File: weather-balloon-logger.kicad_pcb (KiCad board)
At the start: 2 copper layers, 80 x 70 mm, 22 parts, among them J1 Conn_01x02, J2 Conn_01x11, J3 SMA, J4 SMA, J5 Conn_01x02, J6 VHF, J7 HF, Q1 AO3400A, SW1 SPDT, U1 PCF8574T

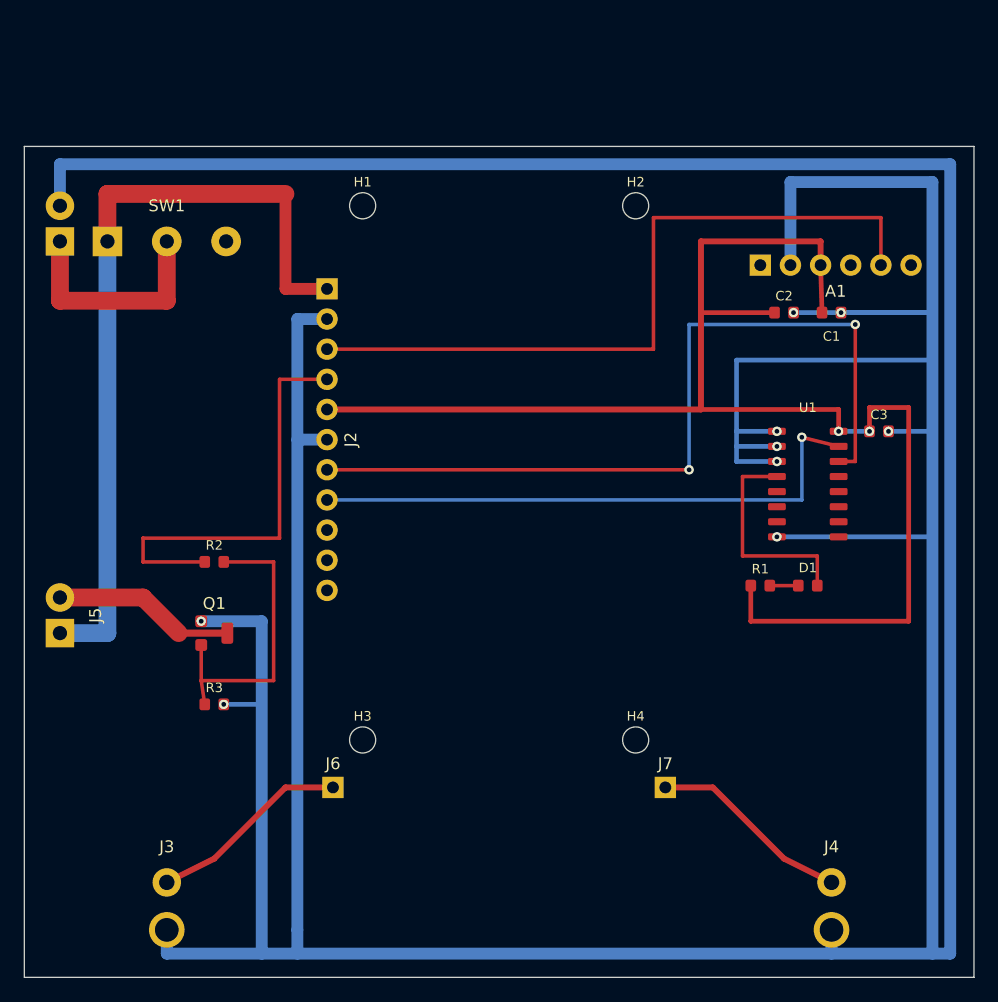
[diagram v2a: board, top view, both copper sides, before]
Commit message: copperhead: Correct the module-mount layout to the exact verified LightAPRS-W 2.0 geometry and FACE-UP orientation in docs/SUBSYSTEMS.md section 6. (1) Resize the module-mount zone to exactly 32.77 x 54.80 mm with the long axis vertical. (2) The module mounts FACE UP, so carrier pads must match the module top view with NO left-right mirror: place J2 (11-pin header) on the zone edge that matches the module's header edge, and place the RF corner contacts as HF bottom-left = J7 and VHF bottom-right = J6, which reverses the previous mirrored placement. (3) Keep RF nets VHF/J6 -> J3 (RF_APRS) and HF/J7 -> J4 (RF_WSPR); the two SMA jacks are edge-mounted facing down, so move J3 toward the VHF/right side and J4 toward the HF/left side for short launches. (4) Place four approximate M2 standoff holes on the dimensioned pattern with about a 42.73 mm outer horizontal span. (5) Keep J1, SW1, A1, U1, C3, Q1 and all passives outside the module zone and honor the >=5 mm SMA keepouts. Update docs/LAYOUT.md and the board, then re-run DRC.
Corrected the LightAPRS-W 2.0 carrier layout to the exact 32.77 x 54.80 mm FACE-UP module zone with its long axis vertical. J2 is on the matching right-hand header edge without mirroring; J7/HF is bottom-left feeding left-side J4/RF_WSPR, and J6/VHF is bottom-right feeding right-side J3/RF_APRS. Four approximate M2 holes use the vendor drawing's about 42.73 mm long-axis span rotated onto the PCB vertical axis. All non-mating components remain outside the zone, both SMA envelopes retain at least 5 mm clearance, documentation and constraints are synchronized, DRC and drift are clean, and the board SVG was refreshed. Draft footprints, exact hole offsets, RF stackup/launches, and physical fit remain explicit fabrication holds.

Verification: ERC clean, DRC clean
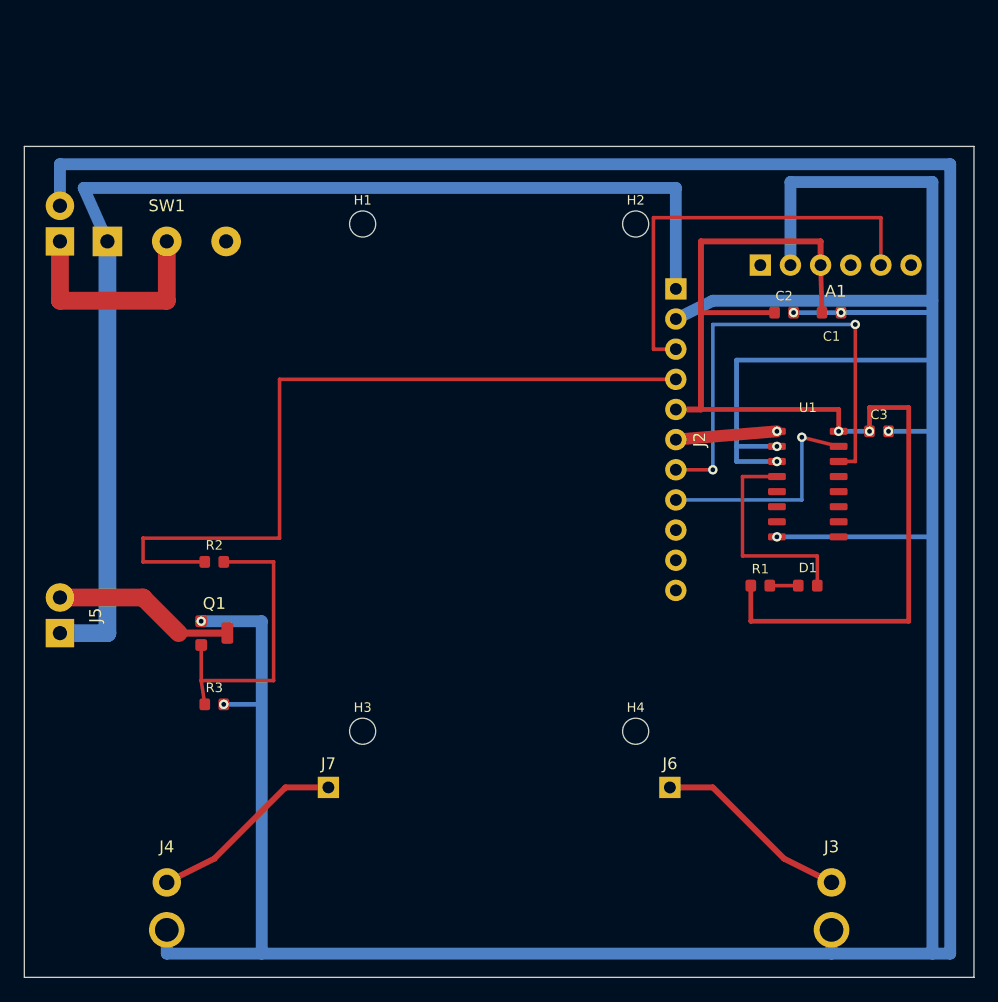
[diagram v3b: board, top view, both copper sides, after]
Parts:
- moved J3 56.0 mm to (168.0, 162.0)
- moved J4 56.0 mm to (112.0, 162.0)
- moved J2 29.4 mm to (154.9, 112.0)
- moved J7 28.4 mm to (125.6, 154.0)
- moved J6 28.4 mm to (154.4, 154.0)
- moved H1 1.53 mm to (128.5, 106.5)
- moved H2 1.53 mm to (151.5, 106.5)
- moved H3 0.74 mm to (128.5, 149.3)
- moved H4 0.74 mm to (151.5, 149.3)
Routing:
- net PACK_SW: track 67.5 -> 100.3 mm
- net I2C_SDA: track 48.5 -> 19.1 mm
- net I2C_SCL: track 69.7 -> 40.3 mm
- net CUTDOWN_CTRL: track 36.1 -> 65.5 mm
- net 3V3: track 123.6 -> 94.2 mm
- net GND: track 465.2 -> 437.2 mm
- net UART_TX: track 61.7 -> 36.1 mm
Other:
- board text added: "LIGHTAPRS-W 2.0 FACE-UP ZONE 32.77 x 54.80 mm"
- board text removed: "LIGHTAPRS-W 2.0 MODULE ZONE 32 x 55 mm"
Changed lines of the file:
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@@
 		(layer "Edge.Cuts")
 	)
-	(gr_rect (start 124 101) (end 156 156)
+	(gr_rect (start 123.615 101) (end 156.385 155.8)
 		(stroke (width 0.3) (type dash))
 		(fill none)
 		(layer "Dwgs.User")
 	)
-	(gr_text "LIGHTAPRS-W 2.0 MODULE ZONE 32 x 55 mm" (at 140 102.5) (layer "Dwgs.User")
+	(gr_text "LIGHTAPRS-W 2.0 FACE-UP ZONE 32.77 x 54.80 mm" (at 140 102.5) (layer "Dwgs.User")
 		(effects (font (size 0.8 0.8) (thickness 0.12)))
 	)
@@
 		(layer "Cmts.User")
 	)
-	(gr_text "APRS 5mm RF CLEARANCE" (at 112 168) (layer "Dwgs.User")
-		(effects (font (size 0.8 0.8) (thickness 0.12)))
-	)
-	(gr_text "WSPR 5mm RF CLEARANCE" (at 168 168) (layer "Dwgs.User")
+	(gr_text "WSPR 5mm RF CLEARANCE" (at 112 168) (layer "Dwgs.User")
+		(effects (font (size 0.8 0.8) (thickness 0.12)))
+	)
+	(gr_text "APRS 5mm RF CLEARANCE" (at 168 168) (layer "Dwgs.User")
 		(effects (font (size 0.8 0.8) (thickness 0.12)))
 	)
@@
 	(footprint "CopperheadDraft_MountingHole_2.2mm"
 		(layer "F.Cu")
-		(at 128.5 105)
+		(at 128.5 106.535)
 		(property "Reference" "H1" (at 0 -2) (layer "F.SilkS") (effects (font (size 0.8 0.8) (thickness 0.12))))
 		(property "Value" "M2_STANDOFF" (at 0 2) (layer "F.Fab") hide (effects (font (size 0.8 0.8) (thickness 0.12))))
@@
 	(footprint "CopperheadDraft_MountingHole_2.2mm"
 		(layer "F.Cu")
-		(at 151.5 105)
+		(at 151.5 106.535)
 		(property "Reference" "H2" (at 0 -2) (layer "F.SilkS") (effects (font (size 0.8 0.8) (thickness 0.12))))
 		(property "Value" "M2_STANDOFF" (at 0 2) (layer "F.Fab") hide (effects (font (size 0.8 0.8) (thickness 0.12))))
@@
 	(footprint "CopperheadDraft_MountingHole_2.2mm"
 		(layer "F.Cu")
-		(at 128.5 150)
+		(at 128.5 149.265)
 		(property "Reference" "H3" (at 0 -2) (layer "F.SilkS") (effects (font (size 0.8 0.8) (thickness 0.12))))
 		(property "Value" "M2_STANDOFF" (at 0 2) (layer "F.Fab") hide (effects (font (size 0.8 0.8) (thickness 0.12))))
@@
 	(footprint "CopperheadDraft_MountingHole_2.2mm"
 		(layer "F.Cu")
-		(at 151.5 150)
+		(at 151.5 149.265)
 		(property "Reference" "H4" (at 0 -2) (layer "F.SilkS") (effects (font (size 0.8 0.8) (thickness 0.12))))
 		(property "Value" "M2_STANDOFF" (at 0 2) (layer "F.Fab") hide (effects (font (size 0.8 0.8) (thickness 0.12))))
@@
 	(footprint "CopperheadDraft_PinHeader_1x11_P2.54mm_Vertical"
 		(layer "F.Cu")
-		(at 125.5 112 270)
+		(at 154.885 112 270)
 		(property "Reference" "J2" (at 12.7 -2 270) (layer "F.SilkS") (effects (font (size 1 1) (thickness 0.15))))
 		(property "Value" "Conn_01x11" (at 12.7 2 270) (layer "F.Fab") hide (effects (font (size 1 1) (thickness 0.15))))
@@
 	(footprint "CopperheadDraft_PinHeader_1x01_P2.54mm_Vertical"
 		(layer "F.Cu")
-		(at 126 154)
+		(at 154.385 154)
 		(property "Reference" "J6" (at 0 -2 0) (layer "F.SilkS") (effects (font (size 1 1) (thickness 0.15))))
 		(property "Value" "VHF" (at 0 2 0) (layer "F.Fab") hide (effects (font (size 1 1) (thickness 0.15))))
@@
 	(footprint "CopperheadDraft_PinHeader_1x01_P2.54mm_Vertical"
 		(layer "F.Cu")
-		(at 154 154)
+		(at 125.615 154)
 		(property "Reference" "J7" (at 0 -2 0) (layer "F.SilkS") (effects (font (size 1 1) (thickness 0.15))))
 		(property "Value" "HF" (at 0 2 0) (layer "F.Fab") hide (effects (font (size 1 1) (thickness 0.15))))
@@
 	(footprint "CopperheadDraft_SMA_Amphenol_132289"
 		(layer "F.Cu")
-		(at 112 162)
+		(at 168 162)
 		(property "Reference" "J3" (at 0 -3 0) (layer "F.SilkS") (effects (font (size 1 1) (thickness 0.15))))
 		(property "Value" "SMA" (at 0 6 0) (layer "F.Fab") hide (effects (font (size 1 1) (thickness 0.15))))
@@
 	(footprint "CopperheadDraft_SMA_Amphenol_132289"
 		(layer "F.Cu")
-		(at 168 162)
+		(at 112 162)
 		(property "Reference" "J4" (at 0 -3 0) (layer "F.SilkS") (effects (font (size 1 1) (thickness 0.15))))
 		(property "Value" "SMA" (at 0 6 0) (layer "F.Fab") hide (effects (font (size 1 1) (thickness 0.15))))
@@
 	(segment (start 103 113) (end 112 113) (width 1.5) (layer "F.Cu") (net 7))
 	(segment (start 112 113) (end 112 108) (width 1.5) (layer "F.Cu") (net 7))
-	(segment (start 107 108) (end 107 104) (width 1.5) (layer "F.Cu") (net 8))
-	(segment (start 107 104) (end 122 104) (width 1.5) (layer "F.Cu") (net 8))
-	(segment (start 122 104) (end 122 112) (width 1) (layer "F.Cu") (net 8))
-	(segment (start 122 112) (end 125.5 112) (width 1) (layer "F.Cu") (net 8))
+	(segment (start 107 108) (end 105 103.5) (width 1) (layer "B.Cu") (net 8))
+	(segment (start 105 103.5) (end 154.885 103.5) (width 1) (layer "B.Cu") (net 8))
+	(segment (start 154.885 103.5) (end 154.885 112) (width 1) (layer "B.Cu") (net 8))
 	(segment (start 107 108) (end 107 141) (width 1.5) (layer "B.Cu") (net 8))
 	(segment (start 107 141) (end 103 141) (width 1.5) (layer "B.Cu") (net 8))
@@
 	(segment (start 110 138) (end 113 141) (width 1.5) (layer "F.Cu") (net 3))
 	(segment (start 113 141) (end 117.1 141) (width 0.6) (layer "F.Cu") (net 3))
-	(segment (start 125.5 119.62) (end 121.5 119.62) (width 0.3) (layer "F.Cu") (net 2))
+	(segment (start 154.885 119.62) (end 121.5 119.62) (width 0.3) (layer "F.Cu") (net 2))
 	(segment (start 121.5 119.62) (end 121.5 133) (width 0.3) (layer "F.Cu") (net 2))
 	(segment (start 121.5 133) (end 110 133) (width 0.3) (layer "F.Cu") (net 2))
@@
 	(segment (start 114.9 145) (end 114.9 142) (width 0.3) (layer "F.Cu") (net 4))
 	(segment (start 114.9 145) (end 115.2 147) (width 0.3) (layer "F.Cu") (net 4))
-	(segment (start 125.5 117.08) (end 153 117.08) (width 0.3) (layer "F.Cu") (net 12))
+	(segment (start 154.885 117.08) (end 153 117.08) (width 0.3) (layer "F.Cu") (net 12))
 	(segment (start 153 117.08) (end 153 106) (width 0.3) (layer "F.Cu") (net 12))
 	(segment (start 153 106) (end 172.16 106) (width 0.3) (layer "F.Cu") (net 12))
 	(segment (start 172.16 106) (end 172.16 110) (width 0.3) (layer "F.Cu") (net 12))
-	(segment (start 125.5 122.16) (end 157 122.16) (width 0.5) (layer "F.Cu") (net 1))
+	(segment (start 154.885 122.16) (end 157 122.16) (width 0.5) (layer "F.Cu") (net 1))
 	(segment (start 157 122.16) (end 157 108) (width 0.5) (layer "F.Cu") (net 1))
 	(segment (start 157 108) (end 167.08 108) (width 0.5) (layer "F.Cu") (net 1))
@@
 	(segment (start 174.5 140) (end 161.2 140) (width 0.4) (layer "F.Cu") (net 1))
 	(segment (start 161.2 140) (end 161.2 137) (width 0.4) (layer "F.Cu") (net 1))
-	(segment (start 125.5 127.24) (end 156 127.24) (width 0.3) (layer "F.Cu") (net 13))
-	(via (at 156 127.24) (size 0.8) (drill 0.4) (layers "F.Cu" "B.Cu") (net 13))
-	(segment (start 156 127.24) (end 156 115) (width 0.3) (layer "B.Cu") (net 13))
-	(segment (start 156 115) (end 170 115) (width 0.3) (layer "B.Cu") (net 13))
+	(segment (start 154.885 127.24) (end 158 127.24) (width 0.3) (layer "F.Cu") (net 13))
+	(via (at 158 127.24) (size 0.8) (drill 0.4) (layers "F.Cu" "B.Cu") (net 13))
+	(segment (start 158 127.24) (end 158 115) (width 0.3) (layer "B.Cu") (net 13))
+	(segment (start 158 115) (end 170 115) (width 0.3) (layer "B.Cu") (net 13))
 	(via (at 170 115) (size 0.8) (drill 0.4) (layers "F.Cu" "B.Cu") (net 13))
 	(segment (start 170 115) (end 170 126.54) (width 0.3) (layer "F.Cu") (net 13))
 	(segment (start 170 126.54) (end 168.6 126.54) (width 0.3) (layer "F.Cu") (net 13))
-	(segment (start 125.5 129.78) (end 165.5 129.78) (width 0.3) (layer "B.Cu") (net 14))
+	(segment (start 154.885 129.78) (end 165.5 129.78) (width 0.3) (layer "B.Cu") (net 14))
 	(segment (start 165.5 129.78) (end 165.5 124.5) (width 0.3) (layer "B.Cu") (net 14))
 	(via (at 165.5 124.5) (size 0.8) (drill 0.4) (layers "F.Cu" "B.Cu") (net 14))
@@
 	(segment (start 164.54 110) (end 164.54 103) (width 1) (layer "B.Cu") (net 5))
 	(segment (start 164.54 103) (end 176.5 103) (width 1) (layer "B.Cu") (net 5))
-	(segment (start 125.5 114.54) (end 123 114.54) (width 1) (layer "B.Cu") (net 5))
-	(segment (start 123 114.54) (end 123 166) (width 1) (layer "B.Cu") (net 5))
-	(segment (start 123 166) (end 123 168) (width 1) (layer "B.Cu") (net 5))
-	(segment (start 125.5 124.7) (end 123 124.7) (width 1) (layer "B.Cu") (net 5))
+	(segment (start 154.885 114.54) (end 158 113) (width 1) (layer "B.Cu") (net 5))
+	(segment (start 158 113) (end 176.5 113) (width 1) (layer "B.Cu") (net 5))
+	(segment (start 154.885 124.7) (end 163.4 124) (width 1) (layer "F.Cu") (net 5))
 	(segment (start 112 166) (end 112 168) (width 1) (layer "B.Cu") (net 5))
 	(segment (start 168 166) (end 168 168) (width 1) (layer "B.Cu") (net 5))
@@
 	(via (at 163.4 132.89) (size 0.8) (drill 0.4) (layers "F.Cu" "B.Cu") (net 5))
 	(segment (start 163.4 132.89) (end 176.5 132.89) (width 0.4) (layer "B.Cu") (net 5))
-	(segment (start 126 154) (end 122 154) (width 0.5) (layer "F.Cu") (net 10))
-	(segment (start 122 154) (end 116 160) (width 0.5) (layer "F.Cu") (net 10))
-	(segment (start 116 160) (end 112 162) (width 0.5) (layer "F.Cu") (net 10))
-	(segment (start 154 154) (end 158 154) (width 0.5) (layer "F.Cu") (net 11))
-	(segment (start 158 154) (end 164 160) (width 0.5) (layer "F.Cu") (net 11))
-	(segment (start 164 160) (end 168 162) (width 0.5) (layer "F.Cu") (net 11))
+	(segment (start 154.385 154) (end 158 154) (width 0.5) (layer "F.Cu") (net 10))
+	(segment (start 158 154) (end 164 160) (width 0.5) (layer "F.Cu") (net 10))
+	(segment (start 164 160) (end 168 162) (width 0.5) (layer "F.Cu") (net 10))
+	(segment (start 125.615 154) (end 122 154) (width 0.5) (layer "F.Cu") (net 11))
+	(segment (start 122 154) (end 116 160) (width 0.5) (layer "F.Cu") (net 11))
+	(segment (start 116 160) (end 112 162) (width 0.5) (layer "F.Cu") (net 11))
 )

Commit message: copperhead: Apply the measured LightAPRS-W 2.0 coordinates from docs/SUBSYSTEMS.md section 6 (Measured coordinate transcription) to the board. (1) Place the four module standoff holes as ~M2 (2.2 mm) holes at H1 (125.9,115.35), H2 (154.1,115.35), H3 (125.9,153.52), H4 (154.1,153.52), forming a 28.18 x 38.16 mm rectangle. (2) Keep J2 (11-pin, 2.548 mm pitch, 270 deg) along the right edge at about x=154.9, centered vertically over the rectangular body, spanning about y=121.7 to 147.2. (3) Keep J7 HF at the module bottom-left and J6 VHF at the module bottom-right, positioned clear of the H3/H4 standoff holes. (4) Keep every other component outside the 32.77 x 54.80 mm module zone and honor the >=5 mm SMA keepouts. Update docs/LAYOUT.md and re-run DRC; iterate placement and routing until DRC is clean.
Applied the measured LightAPRS-W 2.0 module coordinates and documented the result. H1-H4 use 2.2 mm holes at the requested measured coordinates; J2 is centered on the rectangular body at x=154.9 with 2.548 mm pitch and a y=121.72–147.20 span; J7/HF and J6/VHF retain the lower-left/lower-right mapping and use the DRC-clean clearance-adjusted positions (123.7,155.0)/(156.3,155.0). All other components remain outside the module zone, SMA envelopes remain honored, affected routing was reconciled, and the board render was regenerated. ERC clean, DRC clean, and drift clean. Existing physical-coordinate, footprint, RF, and fabrication qualification holds remain explicit.

Verification: ERC clean, DRC clean
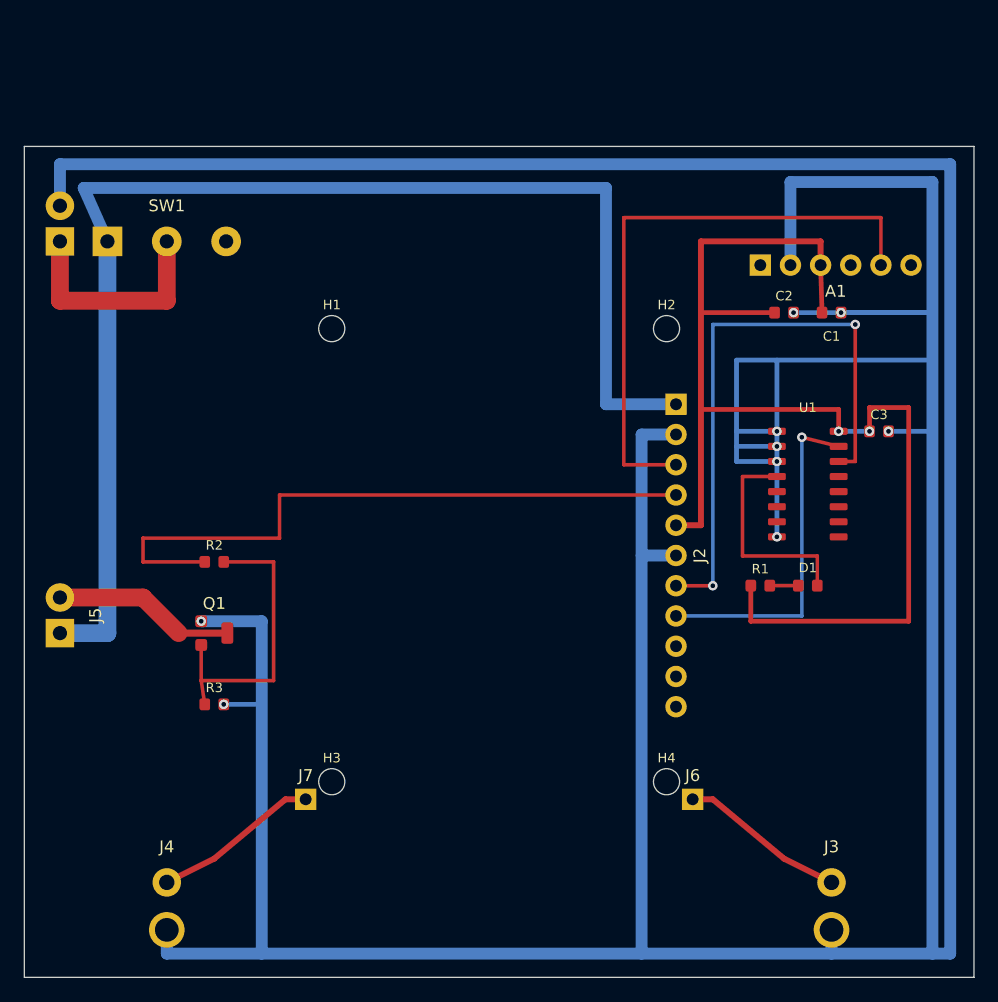
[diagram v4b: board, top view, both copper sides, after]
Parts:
- moved J2 9.72 mm to (154.9, 121.7)
- moved H1 9.19 mm to (125.9, 115.3)
- moved H2 9.19 mm to (154.1, 115.3)
- moved H3 4.99 mm to (125.9, 153.5)
- moved H4 4.99 mm to (154.1, 153.5)
- moved J6 2.16 mm to (156.3, 155.0)
- moved J7 2.16 mm to (123.7, 155.0)
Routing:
- net GND: track 437.2 -> 458.0 mm
- net UART_TX: track 36.1 -> 50.9 mm
- net I2C_SDA: track 19.1 -> 28.9 mm
- net I2C_SCL: track 40.3 -> 50.0 mm
- net 3V3: track 94.2 -> 103.9 mm
- net PACK_SW: track 100.3 -> 110.0 mm
- net CUTDOWN_CTRL: track 65.5 -> 55.7 mm
- net RF_APRS: track 16.6 -> 14.0 mm
- net RF_WSPR: track 16.6 -> 14.0 mm
